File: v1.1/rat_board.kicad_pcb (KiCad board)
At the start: 2 copper layers, 78.7 x 109.2 mm, 23 parts, among them J1 Conn_01x02, J2 Conn_01x04, J3 Conn_01x02, J4 Conn_01x02, J5 Conn_01x02, J6 Conn_01x03, J7 Conn_01x02, J8 Conn_01x02, SW1 SW_SPDT, SW2 SW_Push, U2 DRV8835

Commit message: feat: 基板できた！
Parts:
- removed J4, J8: Conn_01x02, Connector_JST:JST_XH_B2B-XH-A_1x02_P2.50mm_Vertical
- removed REF** (x4): MountingHole_3.2mm_M3, MountingHole:MountingHole_3.2mm_M3
- added BZ1: Buzzer, mori:PKM22EPP-40, F.Cu at (154.0, 87.5)
- added C1: 2.2u, Capacitor_THT:C_Disc_D7.0mm_W2.5mm_P5.00mm, F.Cu at (151.4, 122.0)
- added C2: 0.33u, Capacitor_THT:C_Disc_D7.0mm_W2.5mm_P5.00mm, F.Cu at (146.4, 133.4)
- added H1: MountingHole_Pad, MountingHole:MountingHole_3.2mm_M3_Pad, F.Cu at (108.0, 79.0)
- added H2: MountingHole_Pad, MountingHole:MountingHole_3.2mm_M3_Pad, F.Cu at (170.0, 79.0)
- added H3: MountingHole_Pad, MountingHole:MountingHole_3.2mm_M3_Pad, F.Cu at (170.0, 141.0)
- added H4: MountingHole_Pad, MountingHole:MountingHole_3.2mm_M3_Pad, F.Cu at (108.0, 141.0)
- D1: value LED -> LED BLUE; footprint mori:LED -> LED_THT:LED_D5.0mm
- D2: value LED -> LED WHITE; footprint mori:LED -> LED_THT:LED_D5.0mm
- R3, R4: value 110 -> 470
- U3: value ~ -> NJM2845DL-05
- moved D2 98.0 mm to (117.5, 142.0), turned to 90 degrees
- moved D1 89.1 mm to (125.8, 142.0), turned to 90 degrees
- moved R4 89.1 mm to (119.0, 132.3), turned to 90 degrees
- moved J2 80.7 mm to (159.0, 131.5)
- moved R3 79.1 mm to (126.0, 132.3), turned to 90 degrees
- moved J1 46.5 mm to (169.0, 118.5), turned to 90 degrees
- moved U2 42.4 mm to (151.7, 113.0)
- moved U3 36.8 mm to (153.4, 127.8), turned to 90 degrees
- moved J3 36.3 mm to (169.0, 95.5), turned to 90 degrees
- moved SW2 23.8 mm to (137.2, 139.5), turned to 90 degrees
- moved SW1 23.2 mm to (147.0, 141.0)
- moved R1 23.0 mm to (162.0, 111.0), turned to -90 degrees
- moved J5 22.4 mm to (169.0, 107.0), turned to 90 degrees
- moved J6 21.2 mm to (169.0, 131.0), turned to 90 degrees
- moved R2 18.0 mm to (132.8, 124.7), turned to -90 degrees
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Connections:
- net Net-(J6-Pin_2) renamed RGBLED
- D1 pad 1: Net-(D1-K) -> GND
- D2 pad 1: Net-(D2-K) -> GND
- J1 pad 1: Net-(J1-Pin_1) -> LIMIT_SW
- J2 pad 1: 3.3V -> +3.3V
- J6 pad 1: Net-(J6-Pin_1) -> +5V
- J6 pad 3: Net-(J6-Pin_3) -> GND
- J7 pad 1: +6V -> Net-(J7-Pin_1)
- R1 pad 1: 3.3V -> +3.3V
- R1 pad 2: Net-(J1-Pin_1) -> LIMIT_SW
- R2 pad 1: Net-(U1-IO7) -> +3.3V
- R2 pad 2: Net-(R2-Pad2) -> SW
- R3 pad 1: GND -> Net-(D1-A)
- R3 pad 2: Net-(D1-K) -> LED_A
- R4 pad 1: GND -> Net-(D2-A)
- R4 pad 2: Net-(D2-K) -> LED_B
- SW1 pad 1: +6V -> VCC
- SW1 pad 2: Net-(SW1-B) -> Net-(J7-Pin_1)
- SW2 pad 2: Net-(R2-Pad2) -> SW
- U1 pad 1: 3.3V -> +3.3V
- U1 pad 10: Net-(J1-Pin_1) -> unconnected-(U1-IO26-Pad10)
- U1 pad 11: unconnected-(U1-IO27-Pad11) -> SW
- U1 pad 12: SCL -> LED_A
- U1 pad 13: SDA -> LED_B
- U1 pad 19: Net-(U1-5V) -> +5V
- U1 pad 21: Net-(U1-IO7) -> unconnected-(U1-IO7-Pad21)
- U1 pad 23: Net-(J8-Pin_1) -> LIMIT_SW
- U1 pad 24: Net-(J6-Pin_3) -> unconnected-(U1-IO2-Pad24)
- U1 pad 27: Net-(J6-Pin_1) -> SDA
- U1 pad 28: Net-(J4-Pin_1) -> SCL
- U1 pad 29: unconnected-(U1-IO5-Pad29) -> BIN2
- U1 pad 30: BIN2 -> BIN1
- U1 pad 31: BIN1 -> AIN2
- U1 pad 33: AIN2 -> AIN1
- U1 pad 36: AIN1 -> MODE
- U1 pad 37: MODE -> BUZZER
- U1 pad 7: Net-(D1-A) -> unconnected-(U1-IO32-Pad7)
- U1 pad 8: Net-(D2-A) -> unconnected-(U1-IO33-Pad8)
- U2 pad 1: Net-(SW1-B) -> VCC
- U2 pad 7: 3.3V -> +3.3V
- U3 pad 1: Net-(SW1-B) -> VCC
- U3 pad 3: Net-(U1-5V) -> +5V
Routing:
- net Net-(J1-Pin_1): track 235.1 -> 0.00 mm
- net Net-(SW1-B): track 151.4 -> 0.00 mm
- net +3.3V: track 0.00 -> 146.4 mm
- net 3.3V: track 119.7 -> 0.00 mm
- net +5V: track 0.00 -> 77.9 mm
- net SDA: track 100.7 -> 25.8 mm
- net SCL: track 92.4 -> 25.5 mm
- net VCC: track 0.00 -> 58.7 mm
- net Net-(D2-A): track 44.4 -> 7.77 mm
- net SW: track 0.00 -> 35.1 mm
- net Net-(J6-Pin_3): track 34.8 -> 0.00 mm
- net Net-(J8-Pin_1): track 32.3 -> 0.00 mm
- net LIMIT_SW: track 0.00 -> 32.2 mm
- net Net-(J6-Pin_1): track 28.8 -> 0.00 mm
- net Net-(J4-Pin_1): track 27.1 -> 0.00 mm
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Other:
- board size 78.7 x 109.2 mm -> 70 x 70 mm
- board text added: "Cat-GPT made by Mori"
- board text removed: "Cat-GPT"
- board text removed: "Tool Play Ground"

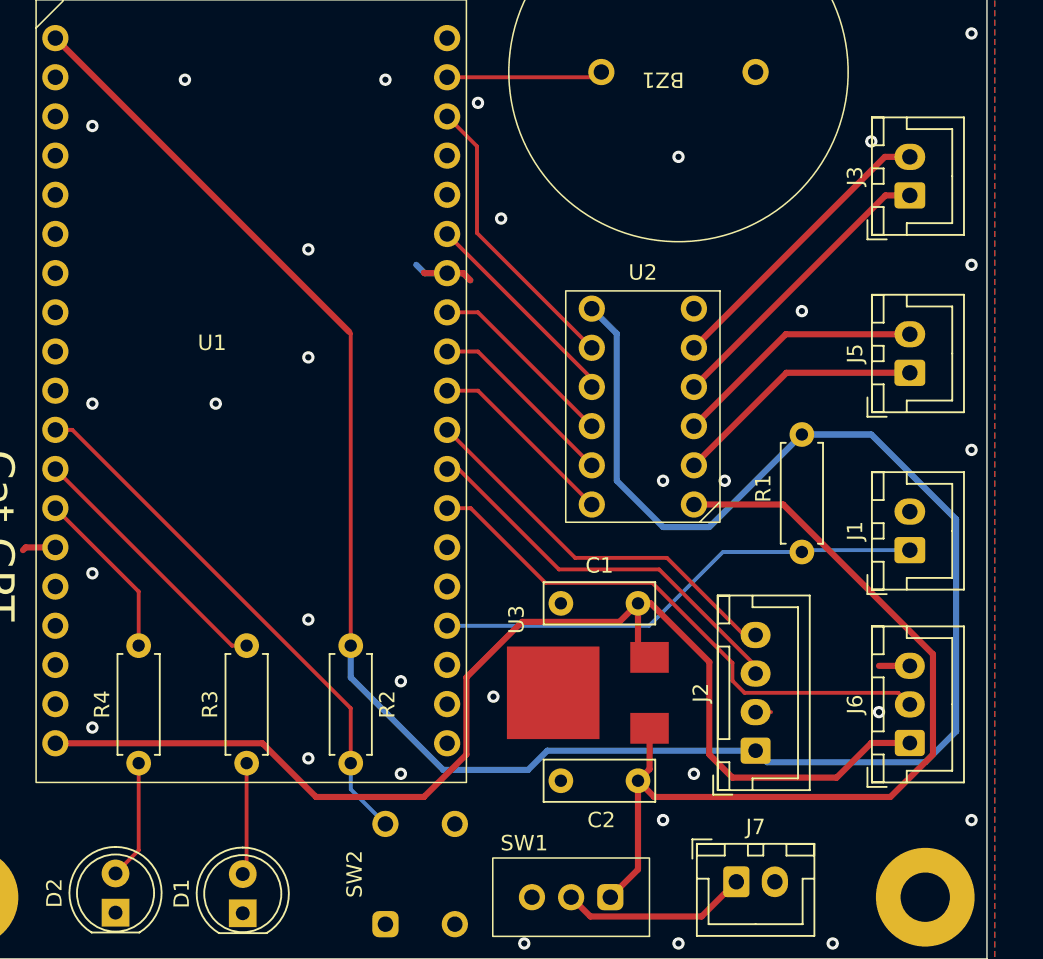
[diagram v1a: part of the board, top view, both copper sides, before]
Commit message: clean: コネクタに接続機器名、素子に規格を記述
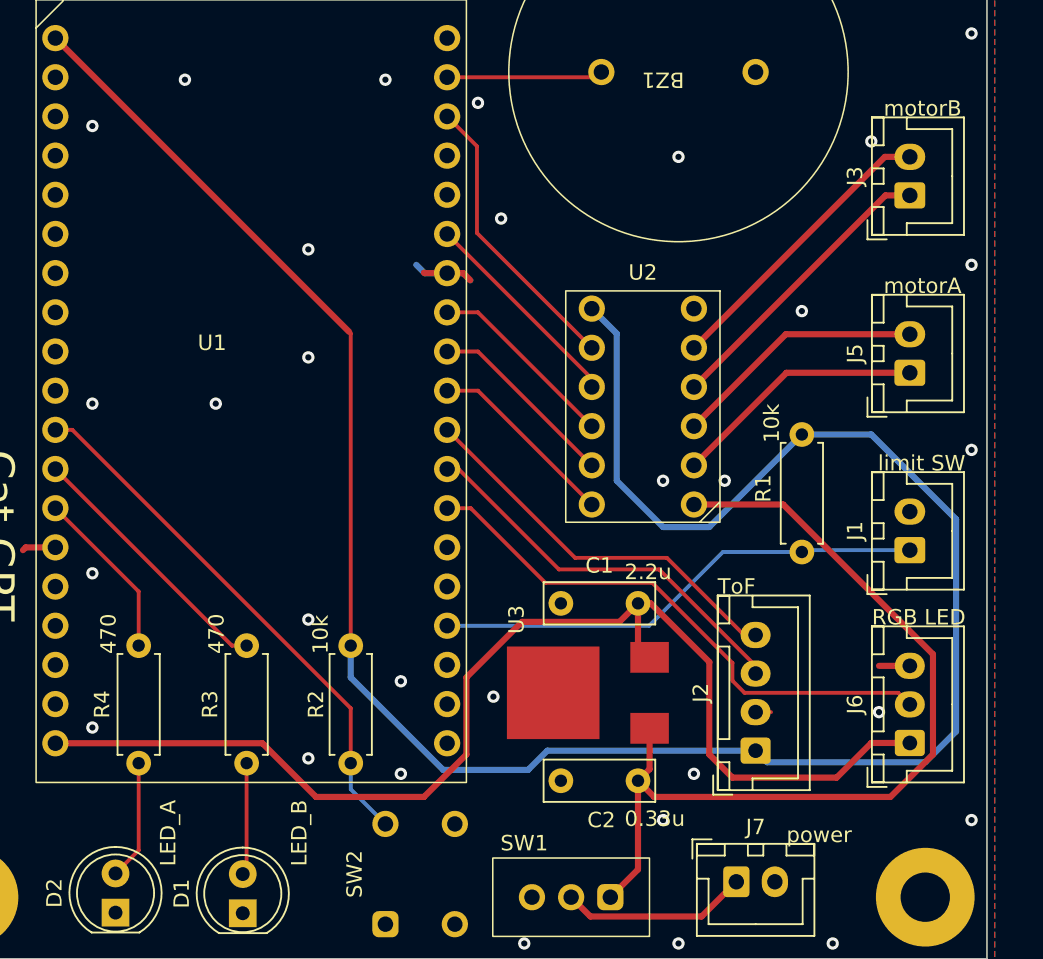
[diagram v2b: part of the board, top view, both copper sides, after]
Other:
- board text added: "0.33u"
- board text added: "10k"
- board text added: "2.2u"
- board text added: "470"
- board text added: "LED_A"
- board text added: "LED_B"
- board text added: "RGB LED"
- board text added: "ToF"
- board text added: "limit SW"
- board text added: "motorA"
- board text added: "motorB"
- board text added: "power"
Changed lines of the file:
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@@
     (property "ki_keywords" "R res resistor")
     (attr through_hole)
-    (fp_text reference "R2" (at 3.81 -2.37 90) (layer "F.SilkS")
+    (fp_text reference "R2" (at 3.81 2.25 90) (layer "F.SilkS")
         (effects (font (size 1 1) (thickness 0.15)))
     )
@@
   (gr_rect (start 104 75) (end 174 145)
     (stroke (width 0.1) (type default)) (fill none) (layer "Edge.Cuts"))
+  (gr_text "LED_B" (at 130 139 90) (layer "F.SilkS")
+    (effects (font (size 1 1) (thickness 0.15)) (justify left bottom))
+  )
+  (gr_text "ToF" (at 156.54 121.44) (layer "F.SilkS")
+    (effects (font (size 1 1) (thickness 0.15)) (justify left bottom))
+  )
+  (gr_text "2.2u" (at 150.5 120.5) (layer "F.SilkS")
+    (effects (font (size 1 1) (thickness 0.15)) (justify left bottom))
+  )
   (gr_text "Cat-GPT\nmade by Mori" (at 105.5 112 270) (layer "F.SilkS")
     (effects (font (size 2 2) (thickness 0.15)) (justify left bottom))
   )
+  (gr_text "RGB LED" (at 166.54 123.44) (layer "F.SilkS")
+    (effects (font (size 1 1) (thickness 0.15)) (justify left bottom))
+  )
+  (gr_text "motorA" (at 167.3 101.95) (layer "F.SilkS")
+    (effects (font (size 1 1) (thickness 0.15)) (justify left bottom))
+  )
+  (gr_text "10k" (at 160.63 111.54 90) (layer "F.SilkS")
+    (effects (font (size 1 1) (thickness 0.15)) (justify left bottom))
+  )
+  (gr_text "LED_A" (at 121.5 139 90) (layer "F.SilkS")
+    (effects (font (size 1 1) (thickness 0.15)) (justify left bottom))
+  )
+  (gr_text "motorB" (at 167.3 90.45) (layer "F.SilkS")
+    (effects (font (size 1 1) (thickness 0.15)) (justify left bottom))
+  )
+  (gr_text "470" (at 117.63 125.23 90) (layer "F.SilkS")
+    (effects (font (size 1 1) (thickness 0.15)) (justify left bottom))
+  )
+  (gr_text "470" (at 124.63 125.23 90) (layer "F.SilkS")
+    (effects (font (size 1 1) (thickness 0.15)) (justify left bottom))
+  )
+  (gr_text "0.33u" (at 150.5 136.5) (layer "F.SilkS")
+    (effects (font (size 1 1) (thickness 0.15)) (justify left bottom))
+  )
+  (gr_text "limit SW" (at 166.925 113.45) (layer "F.SilkS")
+    (effects (font (size 1 1) (thickness 0.15)) (justify left bottom))
+  )
+  (gr_text "power" (at 161 137.55) (layer "F.SilkS")
+    (effects (font (size 1 1) (thickness 0.15)) (justify left bottom))
+  )
+  (gr_text "10k" (at 131.38 125.23 90) (layer "F.SilkS")
+    (effects (font (size 1 1) (thickness 0.15)) (justify left bottom))
+  )
   (dimension (type aligned) (layer "Dwgs.User")
